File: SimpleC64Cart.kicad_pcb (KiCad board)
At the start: 2 copper layers, 58 x 48.9 mm, 12 parts, among them X1 EXPANSION_PORT_C64_EDGE

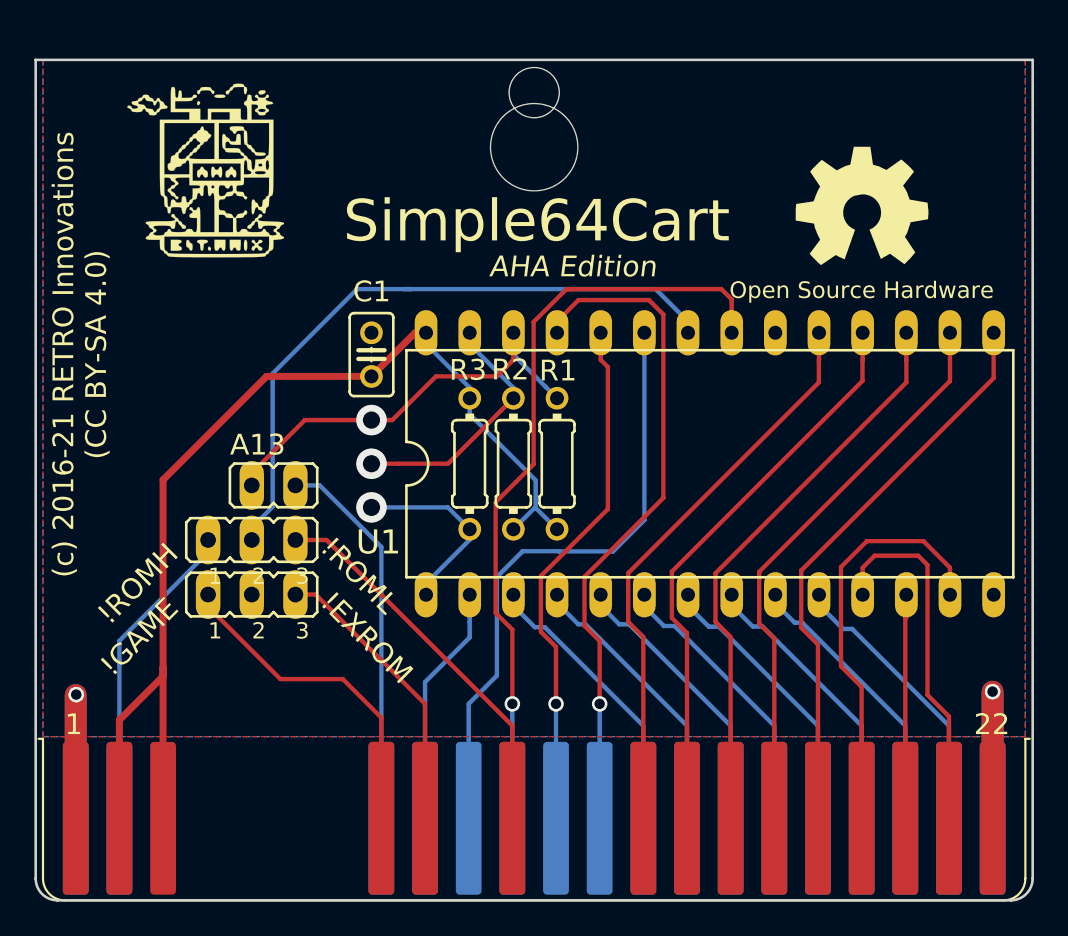
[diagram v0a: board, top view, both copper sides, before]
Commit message: Lengthen board by 1 mm
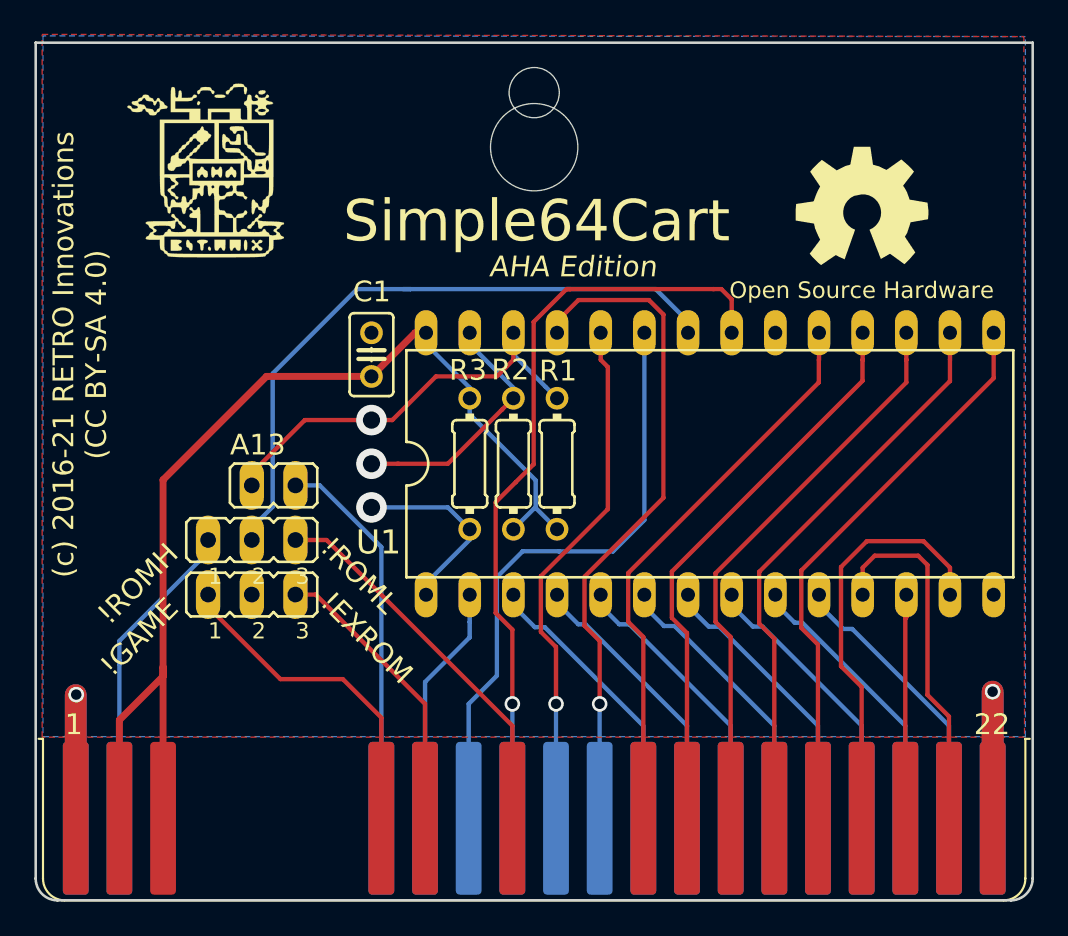
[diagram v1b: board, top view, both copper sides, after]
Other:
- board size 58 x 48.9 mm -> 58 x 49.9 mm
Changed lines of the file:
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@@
     (user_trace_width 1.27)
     (trace_clearance 0.1524)
-    (zone_clearance 0.508)
+    (zone_clearance 0.2)
     (zone_45_only yes)
     (trace_min 0.2)
@@
     (effects (font (size 1.2065 1.2065) (thickness 0.127)) (justify left bottom))
   )
-  (gr_line (start 119.5011 80.5561) (end 119.5011 128.1811) (layer Edge.Cuts) (width 0.15))
+  (gr_line (start 119.5011 79.5561) (end 119.5011 128.1811) (layer Edge.Cuts) (width 0.15))
   (gr_arc (start 120.77 128.18) (end 119.5 128.18) (angle -90) (layer Edge.Cuts) (width 0.15))
   (gr_line (start 120.7711 129.4511) (end 176.2311 129.4511) (layer Edge.Cuts) (width 0.15))
   (gr_arc (start 176.23 128.18) (end 176.23 129.45) (angle -90) (layer Edge.Cuts) (width 0.15))
-  (gr_line (start 177.5011 128.1811) (end 177.5011 80.5561) (layer Edge.Cuts) (width 0.15))
-  (gr_line (start 177.5011 80.5561) (end 119.5011 80.5561) (layer Edge.Cuts) (width 0.15))
+  (gr_line (start 177.5011 128.1811) (end 177.5011 79.5561) (layer Edge.Cuts) (width 0.15))
+  (gr_line (start 177.5011 79.5561) (end 119.5011 79.5561) (layer Edge.Cuts) (width 0.15))
   (segment (start 175.1711 119.2911) (end 175.1711 124.6759) (width 1.27) (layer Bottom) (net 1))
   (segment (start 175.1711 119.2911) (end 175.1711 124.6759) (width 1.27) (layer Top) (net 1))
@@
   (zone (net 1) (net_name GND) (layer Top) (hatch edge 0.508)
     (priority 6)
-    (connect_pads (clearance 0.000001))
+    (connect_pads (clearance 0.2))
     (min_thickness 0.254)
     (fill yes (arc_segments 32) (thermal_gap 0.304) (thermal_bridge_width 0.304))
     (polygon
       (pts
-        (xy 119.9261 80.5561) (xy 177.0761 80.5561) (xy 177.0761 119.9261) (xy 119.9261 119.9261)
+        (xy 119.88 79.072403) (xy 176.989944 79.202403) (xy 177.0261 119.958503) (xy 119.8761 119.958503)
       )
     )
@@
   (zone (net 1) (net_name GND) (layer Bottom) (hatch edge 0.508)
     (priority 6)
-    (connect_pads (clearance 0.000001))
+    (connect_pads (clearance 0.2))
     (min_thickness 0.254)
     (fill yes (arc_segments 32) (thermal_gap 0.304) (thermal_bridge_width 0.304))
     (polygon
       (pts
-        (xy 119.9261 80.5561) (xy 119.9261 119.9261) (xy 177.0761 119.9261) (xy 177.0761 80.5561)
+        (xy 119.9261 79.16) (xy 119.9261 119.9261) (xy 177.0761 119.9261) (xy 177.0761 79.2)
       )
     )

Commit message: Modified pcb layout.
	* support 16k rom images
	* jumpers allow using 1 of 4 16k banks
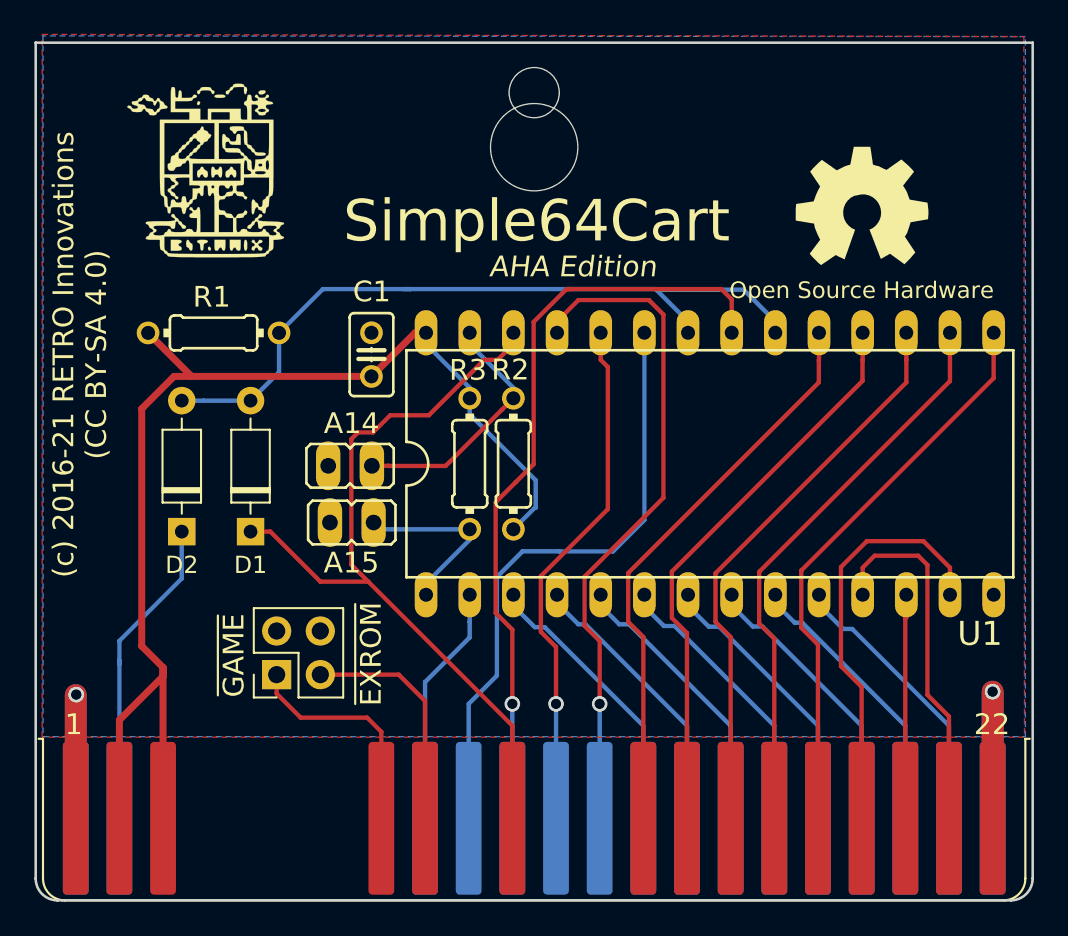
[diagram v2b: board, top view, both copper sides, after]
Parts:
- removed A13: , JP1
- removed JP1, JP2: , JP2
- added A14: , JP1, F.Cu at (137.8, 104.2)
- added A15: , JP1, F.Cu at (137.9, 107.5)
- added D1: D_DO-35_SOD27_P7.62mm_Horizontal, Diode_THT:D_DO-35_SOD27_P7.62mm_Horizontal, F.Cu at (132.0, 108.0)
- added D2: D_DO-35_SOD27_P7.62mm_Horizontal, Diode_THT:D_DO-35_SOD27_P7.62mm_Horizontal, F.Cu at (128.0, 108.0)
- added TYPE: PinHeader_2x02_P2.54mm_Vertical, Connector_PinHeader_2.54mm:PinHeader_2x02_P2.54mm_Vertical, F.Cu at (133.5, 116.3)
- moved R1 21.4 mm to (129.8, 96.4), turned to 0 degrees
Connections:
- R1 pad 2: ADDR13 -> N$1
- U1 pad 20: GND -> N$1
- U1 pad 26: ADDR13 -> ~ROML
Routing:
- net ADDR13: track 25.1 -> 0.00 mm, vias 1 -> 0
- net ~ROML: track 22.5 -> 46.4 mm
- net A13: track 23.5 -> 0.00 mm
- net ~GAME: track 23.4 -> 17.3 mm
- net VCC: track 64.8 -> 70.8 mm
- net N$1: track 38.3 -> 43.7 mm
- net ~EXROM: track 16.8 -> 13.6 mm
- net GND: track 30.3 -> 29.1 mm
- net ADDR15: track 11.1 -> 10.6 mm, vias 1 -> 0
- net ADDR14: vias 1 -> 0
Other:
- board text added: "~EXROM"
- board text added: "~GAME"
- board text removed: "!EXROM"
- board text removed: "!GAME"
- board text removed: "!ROMH"
- board text removed: "!ROML"

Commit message: Add schematic for board layout
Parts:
- A14, A15: value (none) -> Conn_01x02_Male
- C1: value (none) -> 0.1uf
- D1, D2: value D_DO-35_SOD27_P7.62mm_Horizontal -> D_Small
- J1: renamed from TYPE; value PinHeader_2x02_P2.54mm_Vertical -> TYPE
- R1, R2, R3: value (none) -> 10k
- U1: value (none) -> 27512G
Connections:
- net A0 renamed /A0
- net A1 renamed /A1
- net A10 renamed /A10
- net A11 renamed /A11
- net A12 renamed /A12
- net A13 renamed /A13
- net A14 renamed /A14
- net A15 renamed /A15
- net A2 renamed /A2
- net A3 renamed /A3
- net A4 renamed /A4
- net A5 renamed /A5
- net A6 renamed /A6
- net A7 renamed /A7
- net A8 renamed /A8
- net A9 renamed /A9
- net ADDR14 renamed Net-(A14-Pad2)
- net ADDR15 renamed Net-(A15-Pad2)
- net BA renamed /BA
- net D0 renamed /D0
- net D1 renamed /D1
- net D2 renamed /D2
- net D3 renamed /D3
- net D4 renamed /D4
- net D5 renamed /D5
- net D6 renamed /D6
- net D7 renamed /D7
- net DOTCLK renamed /DOTCLK
- net PHI2 renamed /PHI2
- net R/~W renamed /R\~W
- net ~DMA renamed /~DMA
- net ~EXROM renamed /~EXROM
- net ~GAME renamed /~GAME
- net ~IO1 renamed /~IO1
- net ~IO2 renamed /~IO2
- net ~IRQ renamed /~IRQ
- net ~NMI renamed /~NMI
- net ~RESET renamed /~RESET
- net ~ROMH renamed /~ROMH
- net ~ROML renamed /~ROML
